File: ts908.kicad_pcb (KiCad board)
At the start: 2 copper layers, 41.3 x 55.9 mm, 56 parts, among them Q1 2SC1815, Q2 2SC1815, U1 RC4559

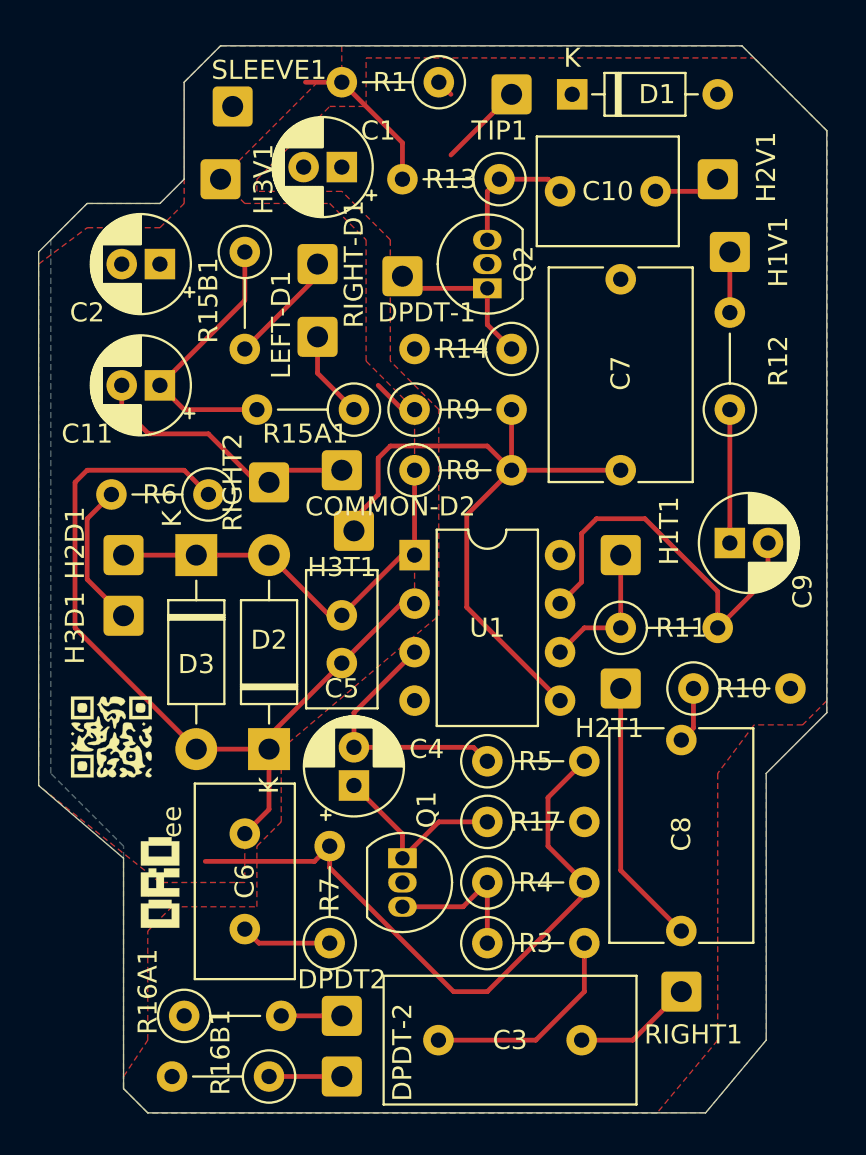
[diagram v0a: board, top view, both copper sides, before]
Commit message: Fixed wrong silks and missing R2
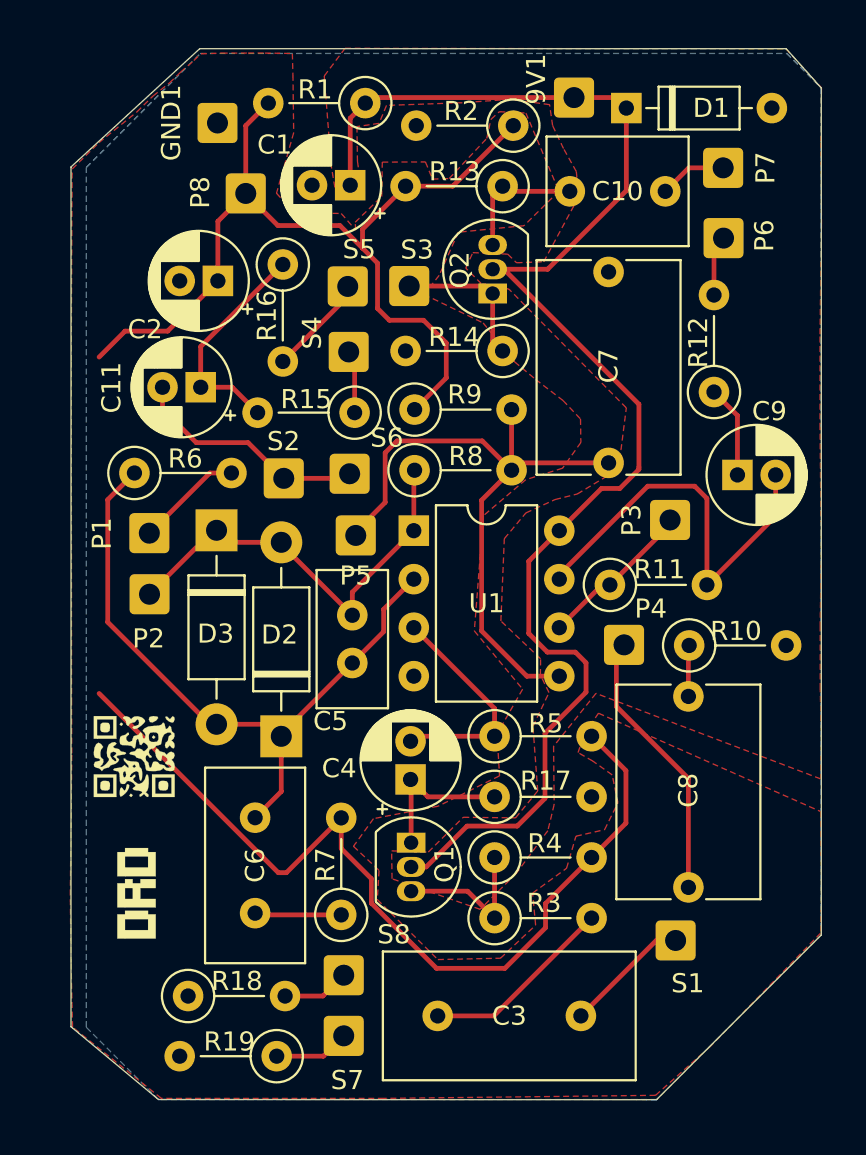
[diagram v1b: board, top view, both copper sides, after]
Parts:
- removed COMMON-D2: DPDT-2, Connector_Wire:SolderWire-0.5sqmm_1x01_D0.9mm_OD2.1mm
- removed R16B1: 100K, Resistor_THT:R_Axial_DIN0207_L6.3mm_D2.5mm_P5.08mm_Vertical
- removed SLEEVE1: DC-JACK, Connector_Wire:SolderWire-0.5sqmm_1x01_D0.9mm_OD2.1mm
- added GND1: DC-JACK, Connector_Wire:SolderWire-0.5sqmm_1x01_D0.9mm_OD2.1mm, F.Cu at (236.1, 85.3)
- added R19: 100K, Resistor_THT:R_Axial_DIN0207_L6.3mm_D2.5mm_P5.08mm_Vertical, F.Cu at (239.2, 134.2)
- added R2: 10K, Resistor_THT:R_Axial_DIN0207_L6.3mm_D2.5mm_P5.08mm_Vertical, F.Cu at (251.6, 85.5)
- added S6: DPDT B-COMM, Connector_Wire:SolderWire-0.5sqmm_1x01_D0.9mm_OD2.1mm, F.Cu at (243.0, 103.7)
- P1: renamed from H3D1; value DRIVE -> DRIVE POT 3
- P2: renamed from H2D1; value DRIVE -> DRIVE POT 2
- P3: renamed from H1T1; value TONE -> TONE POT 1
- P4: renamed from H2T1; value TONE -> TONE POT 2
- P5: renamed from H3T1; value TONE -> TONE POT 3
- P6: renamed from H1V1; value VOL -> VOL POT 1
- P7: renamed from H2V1; value VOL -> VOL POT 2
- P8: renamed from H3V1; value VOL -> VOL POT 3
- S1: renamed from RIGHT1; value 3PDT-1 -> 3PDT A-LEFT
- S2: renamed from RIGHT2; value 3PDT-2 -> 3PDT A-RIGHT
- S3: renamed from DPDT-1; value COMMON-D1 -> DPDT A-COMM
- S4: renamed from LEFT-D1; value DPDT-1 -> DPDT A-LEFT
- S5: renamed from RIGHT-D1; value DPDT-1 -> DPDT A-RIGHT
- S7: renamed from DPDT-2; value LEFT-D2 -> DPDT B-LEFT
- S8: renamed from DPDT2; value RIGHT-D2 -> DPDT B-RIGHT
- moved P1 4.53 mm to (232.5, 106.8)
- moved R6 4.04 mm to (231.7, 103.7), turned to 0 degrees
- moved R1 4.00 mm to (243.8, 84.3)
- moved C9 3.59 mm to (263.3, 103.8)
- moved 9V1 3.27 mm to (254.7, 84.0), turned to 90 degrees
- moved P3 3.17 mm to (259.8, 106.1)
- moved C2 3.16 mm to (236.1, 93.6)
- moved C4 2.98 mm to (246.2, 119.7)
- moved D1 2.93 mm to (257.5, 84.5)
- moved S1 2.70 mm to (260.1, 128.1)
- moved P2 2.46 mm to (232.5, 110.0)
- moved R11 2.32 mm to (256.6, 109.5)
- moved C8 2.31 mm to (260.7, 125.3)
- moved P4 2.29 mm to (257.4, 112.7)
- moved R10 2.27 mm to (260.8, 112.7)
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- renumbered TIP1 to 9V1, R15A1 to R15, R15B1 to R16, R16A1 to R18
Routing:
- net +9V: track 5.39 -> 77.9 mm
- net VCC: track 45.4 -> 95.5 mm
- net Net-(C5-Pad2): track 44.3 -> 35.9 mm
- net Net-(C11-Pad1): track 14.4 -> 11.7 mm
- net Net-(C9-Pad1): track 6.98 -> 4.85 mm
- net Net-(P1-Pad1): track 7.67 -> 5.60 mm
- net Net-(C11-Pad2): track 14.6 -> 12.5 mm
- net Net-(C4-Pad1): track 10.1 -> 8.10 mm
- net Net-(C7-Pad1): track 36.8 -> 35.0 mm
- net Net-(C4-Pad2): track 13.6 -> 11.9 mm
- net Net-(C9-Pad2): track 20.6 -> 21.9 mm
- net Net-(R15-Pad1): track 4.60 -> 3.31 mm
- net Net-(C3-Pad1): track 11.2 -> 10.2 mm
- net Net-(P3-Pad1): track 7.51 -> 8.28 mm
- net Net-(R16-Pad2): track 6.02 -> 5.34 mm
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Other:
- board size 41.3 x 55.9 mm -> 39.3 x 55 mm
- board text removed: "ee"

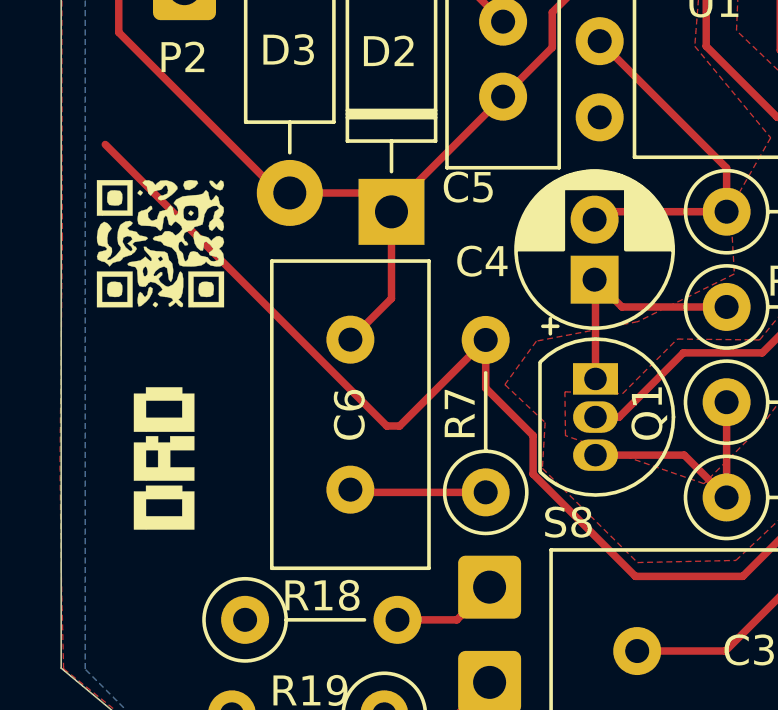
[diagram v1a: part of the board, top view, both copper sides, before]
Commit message: More silks, better qr-code, 3d render
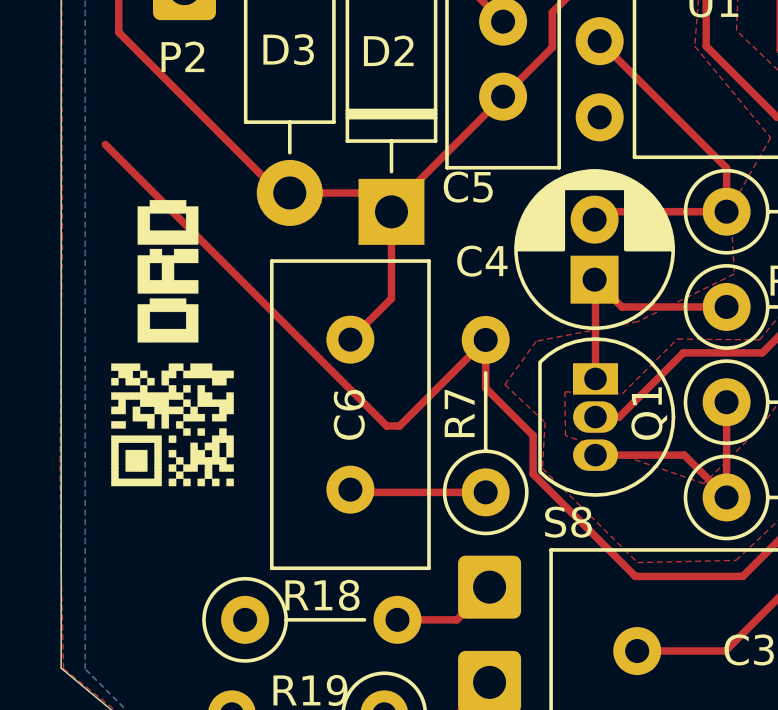
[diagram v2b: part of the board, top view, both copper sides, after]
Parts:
- removed the G*** at (231.7, 118.5)
- added QR-Code: , ts908:QR-Code, F.Cu at (230.1, 126.6)
- added TS908: , ts908:ts908-resize, B.Cu at (230.1, 119.0)
- moved G*** 6.24 mm to (231.9, 119.4)

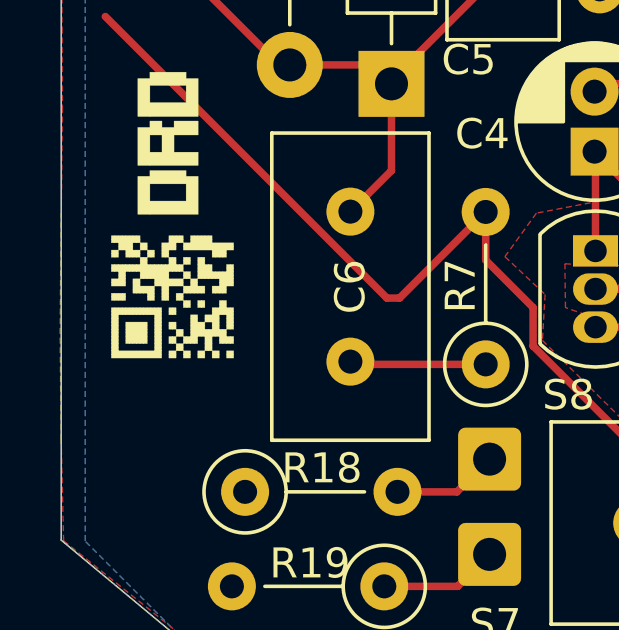
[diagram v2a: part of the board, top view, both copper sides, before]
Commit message: Fixed QR Code
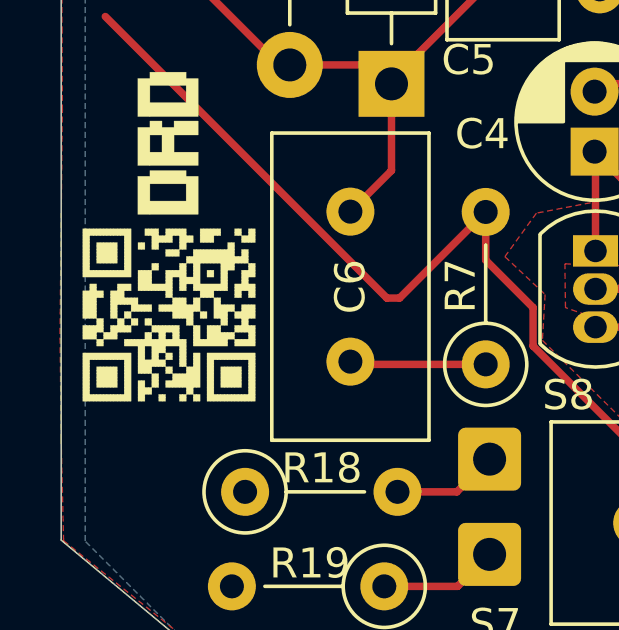
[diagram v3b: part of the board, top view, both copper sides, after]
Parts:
- removed QR-Code: , ts908:QR-Code
- added TS908: , ts908:QR-Code, F.Cu at (229.1, 128.0)
